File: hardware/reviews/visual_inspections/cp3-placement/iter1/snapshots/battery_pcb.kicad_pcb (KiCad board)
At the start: 2 copper layers, 100 x 80 mm, 127 parts, among them J1 Phoenix_MSTBA_2,5-2-G-5,08, J10 Amphenol_RJHSE-5380, J11 Amphenol_RJHSE-5380, J2 Amphenol_RJHSE-5380, J3 USB-C 2.0, J4 TERM, J5 ESP-Prog, J6 Amphenol_RJHSE-5380, J7 TERM, Q10 NTR4171P, Q11 NTR4171P, Q3 2N7002, Q4 2N7002, Q5 NTR4171P, U1 LM5166YDRCR, U10 ADM2587EBRWZ, U11 ADM2587EBRWZ, U2 R-78HB12-0.5, U3 THVD1400DR, U4 TPS3808G01DBVR, U5 AP2112K-3.3, U6 TPS2116DRLR, U7 TCAN332DR

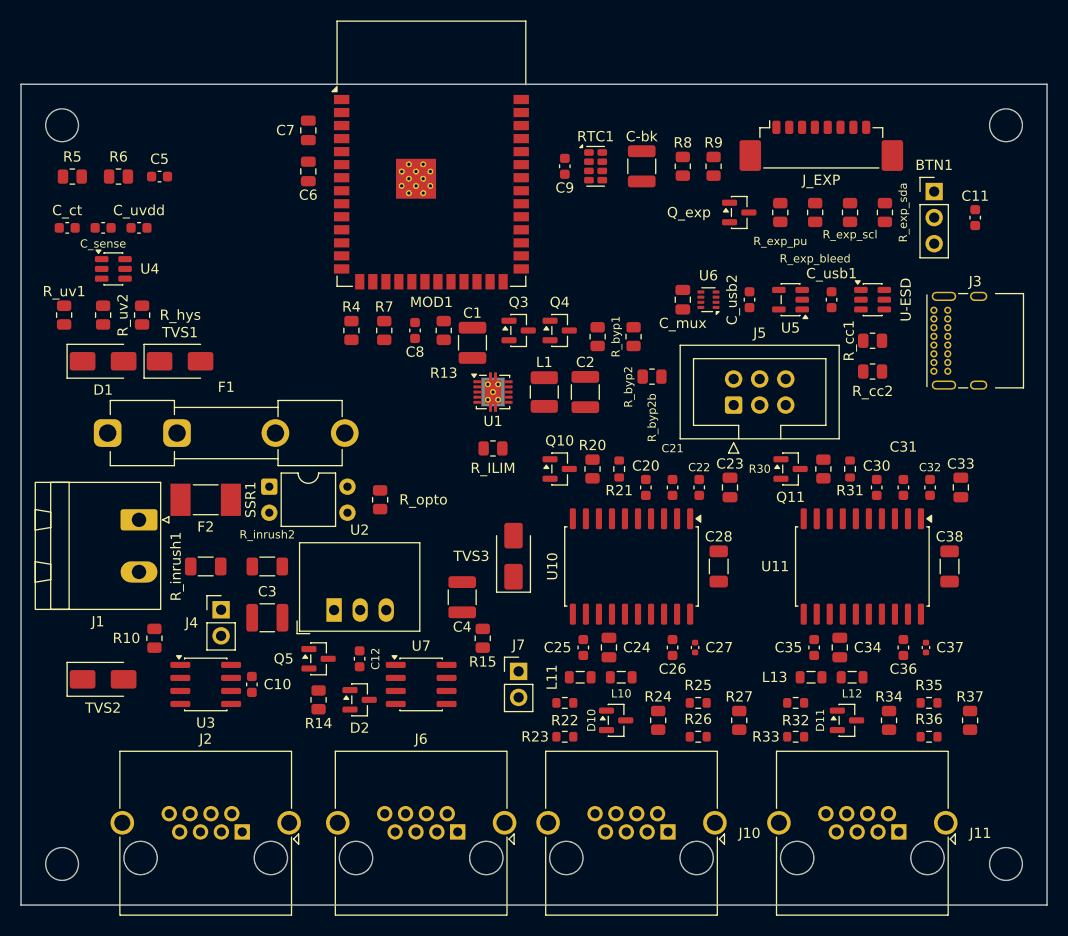
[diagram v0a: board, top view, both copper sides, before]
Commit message: cp3: post-handoff adversarial self-review (packet 4.5) — silk floored at JLC 1.0/0.15 min with dense-row re-space to 0 silk findings, DRC-oracle refdes refine loop, D1/TVS1 current-path fix, Phoenix 1757242 header verified, honest packet claims
Co-Authored-By: Claude Fable 5 <noreply@anthropic.com>
Claude-Session: https://claude.ai/code/session_01EP34oLvQKnuhf59mAfUYQf
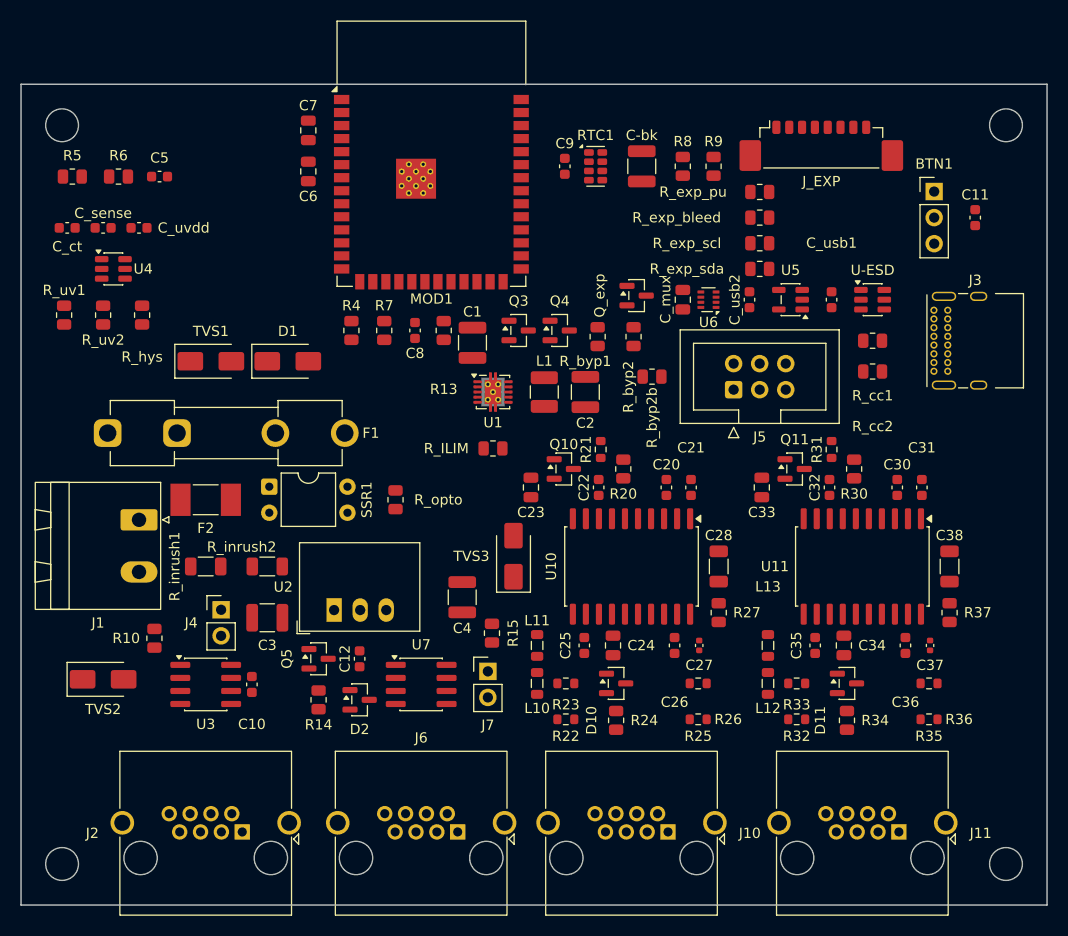
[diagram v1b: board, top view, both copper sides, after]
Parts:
- moved C23 19.4 mm to (49.7, 39.3)
- moved C33 19.4 mm to (72.2, 39.3)
- moved D1 18.0 mm to (26.0, 27.0)
- moved R_exp_sda 13.4 mm to (72.0, 18.0), turned to 0 degrees
- moved Q_exp 12.9 mm to (60.0, 20.6)
- moved R27 10.7 mm to (68.0, 51.5)
- moved R37 10.7 mm to (90.5, 51.5)
- moved C22 9.80 mm to (56.3, 39.3)
- moved C32 9.80 mm to (78.8, 39.3)
- moved R_exp_scl 9.30 mm to (72.0, 15.5), turned to 0 degrees
- moved L10 8.22 mm to (50.3, 58.4), turned to 90 degrees
- moved L12 8.22 mm to (72.8, 58.4), turned to 90 degrees
- moved R_exp_bleed 5.42 mm to (72.0, 13.0), turned to 0 degrees
- moved L11 5.22 mm to (50.3, 54.7), turned to 90 degrees
- moved L13 5.22 mm to (72.8, 54.7), turned to 90 degrees
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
